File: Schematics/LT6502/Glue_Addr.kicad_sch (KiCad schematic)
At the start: 28 parts, among them IC1 ATF1508AS-7AX100, J1 Conn_02x05_Odd_Even, X1 28.322MHz

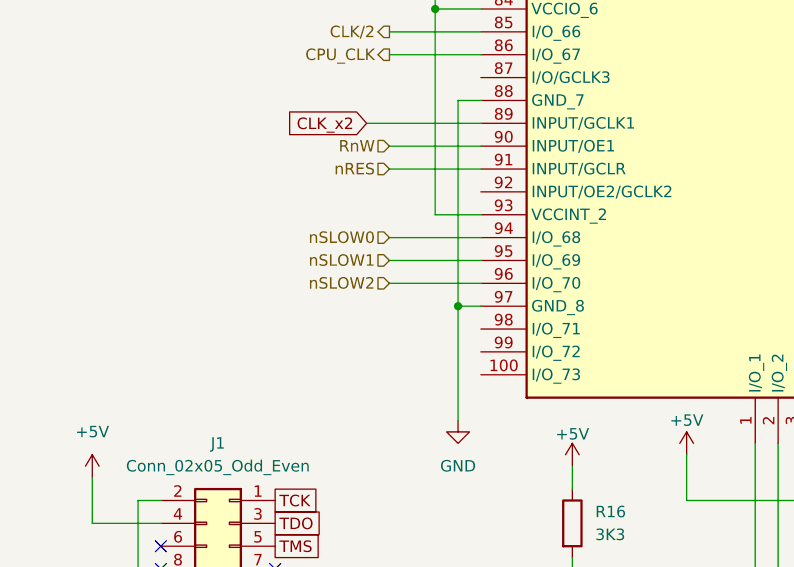
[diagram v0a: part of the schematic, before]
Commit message: Tweaks to Schematics
Shrunk main PCB
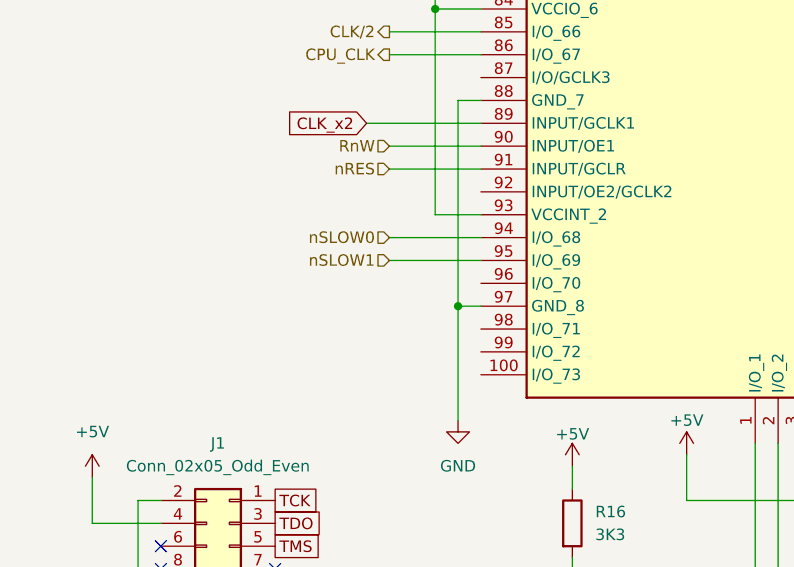
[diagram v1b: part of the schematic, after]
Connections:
- net nSLOW2: no longer names the net of IC1.96 (I/O_70)
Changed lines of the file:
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@@
-	(wire
-		(pts
-			(xy 57.15 97.79) (xy 67.31 97.79)
-		)
-		(stroke
-			(width 0)
-			(type default)
-		)
-	)
 	(wire
 		(pts
@@
 		)
 	)
-	(hierarchical_label "nSLOW2"
-		(shape input)
-		(at 57.15 97.79 180)
-		(effects
-			(font
-				(size 1.27 1.27)
-			)
-			(justify right)
-		)
-	)

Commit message: Further work on Schematics, All parts placed on PCB
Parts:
- J1: footprint Connector_PinHeader_2.54mm:PinHeader_2x05_P2.54mm_Vertical -> Connector_PinHeader_2.54mm:PinHeader_2x05_P2.54mm_Horizontal
- R14, R15, R16, R17, R18, R19, R20, R21, R22, R23, R24, R25, R26, R27, R28: footprint Resistor_SMD:R_0603_1608Metric_Pad0.98x0.95mm_HandSolder -> Resistor_SMD:R_0402_1005Metric
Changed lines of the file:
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@@
 			)
 		)
-		(property "Footprint" "Resistor_SMD:R_0603_1608Metric_Pad0.98x0.95mm_HandSolder"
+		(property "Footprint" "Resistor_SMD:R_0402_1005Metric"
 			(at 229.362 50.8 90)
 			(effects
@@
 			)
 		)
-		(property "Footprint" "Resistor_SMD:R_0603_1608Metric_Pad0.98x0.95mm_HandSolder"
+		(property "Footprint" "Resistor_SMD:R_0402_1005Metric"
 			(at 136.652 137.16 90)
 			(effects
@@
 			)
 		)
-		(property "Footprint" "Resistor_SMD:R_0603_1608Metric_Pad0.98x0.95mm_HandSolder"
+		(property "Footprint" "Resistor_SMD:R_0402_1005Metric"
 			(at 235.712 115.57 90)
 			(effects
@@
 			)
 		)
-		(property "Footprint" "Resistor_SMD:R_0603_1608Metric_Pad0.98x0.95mm_HandSolder"
+		(property "Footprint" "Resistor_SMD:R_0402_1005Metric"
 			(at 179.832 151.13 90)
 			(effects
@@
 			)
 		)
-		(property "Footprint" "Connector_PinHeader_2.54mm:PinHeader_2x05_P2.54mm_Vertical"
+		(property "Footprint" "Connector_PinHeader_2.54mm:PinHeader_2x05_P2.54mm_Horizontal"
 			(at 39.37 127 0)
 			(effects
@@
 			)
 		)
-		(property "Footprint" "Resistor_SMD:R_0603_1608Metric_Pad0.98x0.95mm_HandSolder"
+		(property "Footprint" "Resistor_SMD:R_0402_1005Metric"
 			(at 75.692 124.46 90)
 			(effects
@@
 			)
 		)
-		(property "Footprint" "Resistor_SMD:R_0603_1608Metric_Pad0.98x0.95mm_HandSolder"
+		(property "Footprint" "Resistor_SMD:R_0402_1005Metric"
 			(at 214.122 50.8 90)
 			(effects
@@
 			)
 		)
-		(property "Footprint" "Resistor_SMD:R_0603_1608Metric_Pad0.98x0.95mm_HandSolder"
+		(property "Footprint" "Resistor_SMD:R_0402_1005Metric"
 			(at 132.842 157.48 90)
 			(effects
@@
 			)
 		)
-		(property "Footprint" "Resistor_SMD:R_0603_1608Metric_Pad0.98x0.95mm_HandSolder"
+		(property "Footprint" "Resistor_SMD:R_0402_1005Metric"
 			(at 225.552 115.57 90)
 			(effects
@@
 			)
 		)
-		(property "Footprint" "Resistor_SMD:R_0603_1608Metric_Pad0.98x0.95mm_HandSolder"
+		(property "Footprint" "Resistor_SMD:R_0402_1005Metric"
 			(at 50.038 43.18 90)
 			(effects
@@
 			)
 		)
-		(property "Footprint" "Resistor_SMD:R_0603_1608Metric_Pad0.98x0.95mm_HandSolder"
+		(property "Footprint" "Resistor_SMD:R_0402_1005Metric"
 			(at 203.962 50.8 90)
 			(effects
@@
 			)
 		)
-		(property "Footprint" "Resistor_SMD:R_0603_1608Metric_Pad0.98x0.95mm_HandSolder"
+		(property "Footprint" "Resistor_SMD:R_0402_1005Metric"
 			(at 215.392 115.57 90)
 			(effects
@@
 			)
 		)
-		(property "Footprint" "Resistor_SMD:R_0603_1608Metric_Pad0.98x0.95mm_HandSolder"
+		(property "Footprint" "Resistor_SMD:R_0402_1005Metric"
 			(at 24.638 165.1 90)
 			(effects
@@
 			)
 		)
-		(property "Footprint" "Resistor_SMD:R_0603_1608Metric_Pad0.98x0.95mm_HandSolder"
+		(property "Footprint" "Resistor_SMD:R_0402_1005Metric"
 			(at 167.132 151.13 90)
 			(effects
@@
 			)
 		)
-		(property "Footprint" "Resistor_SMD:R_0603_1608Metric_Pad0.98x0.95mm_HandSolder"
+		(property "Footprint" "Resistor_SMD:R_0402_1005Metric"
 			(at 243.332 50.8 90)
 			(effects
@@
 			)
 		)
-		(property "Footprint" "Resistor_SMD:R_0603_1608Metric_Pad0.98x0.95mm_HandSolder"
+		(property "Footprint" "Resistor_SMD:R_0402_1005Metric"
 			(at 253.492 50.8 90)
 			(effects

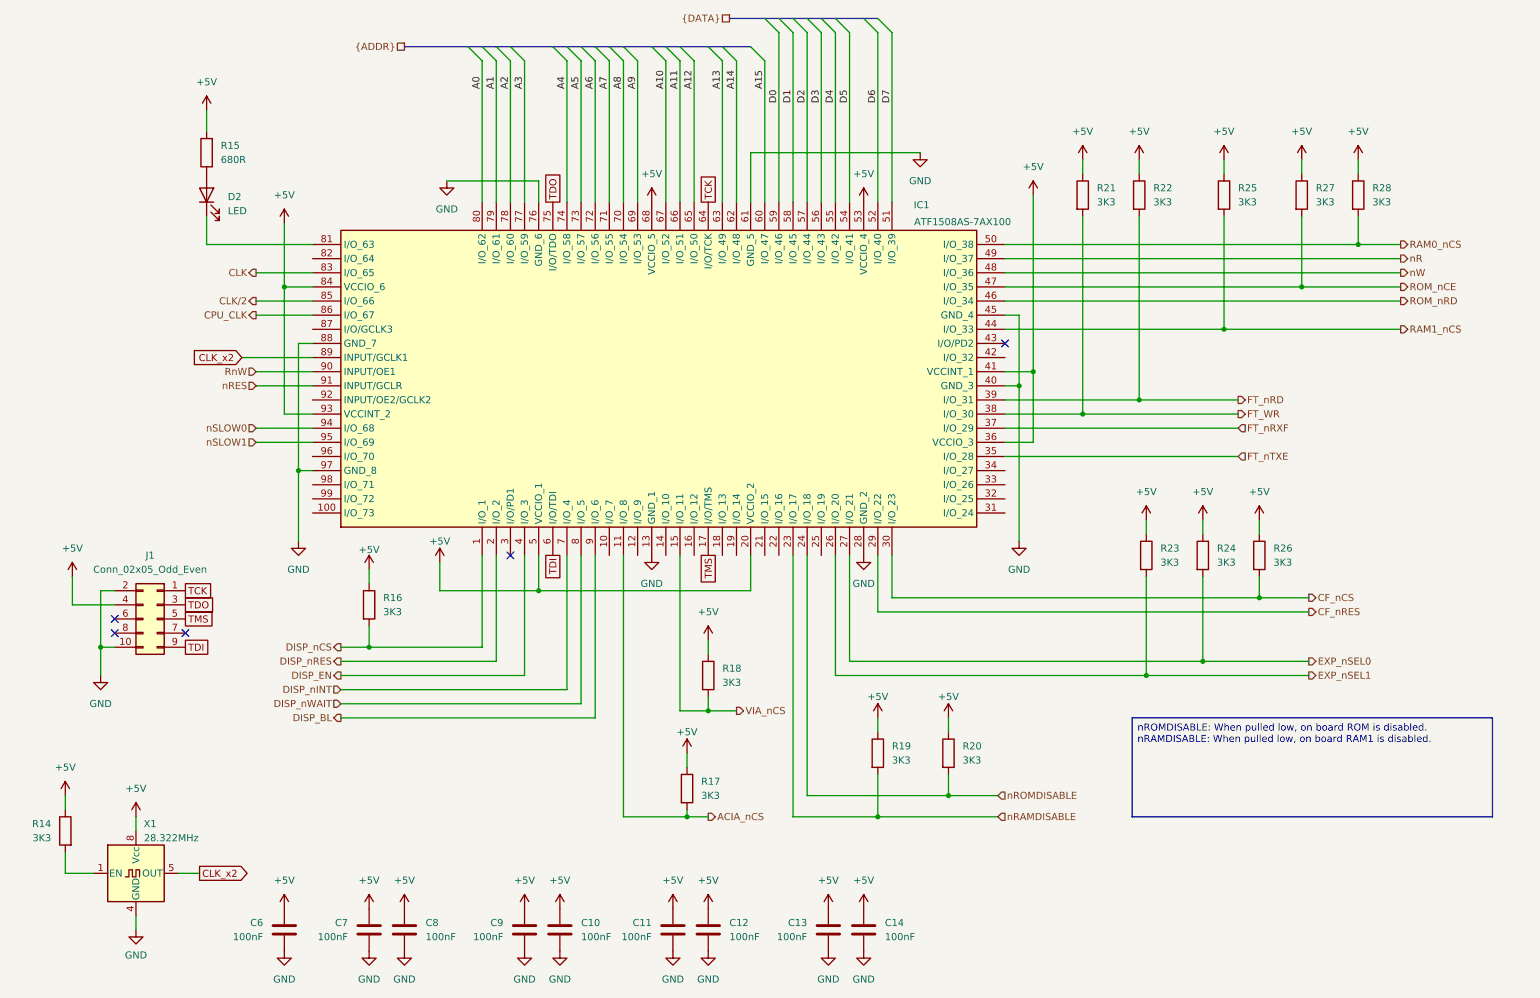
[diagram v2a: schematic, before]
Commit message: Updated main board and started keybed
main board a bit wider due to keybed width
created keybed, begun routing
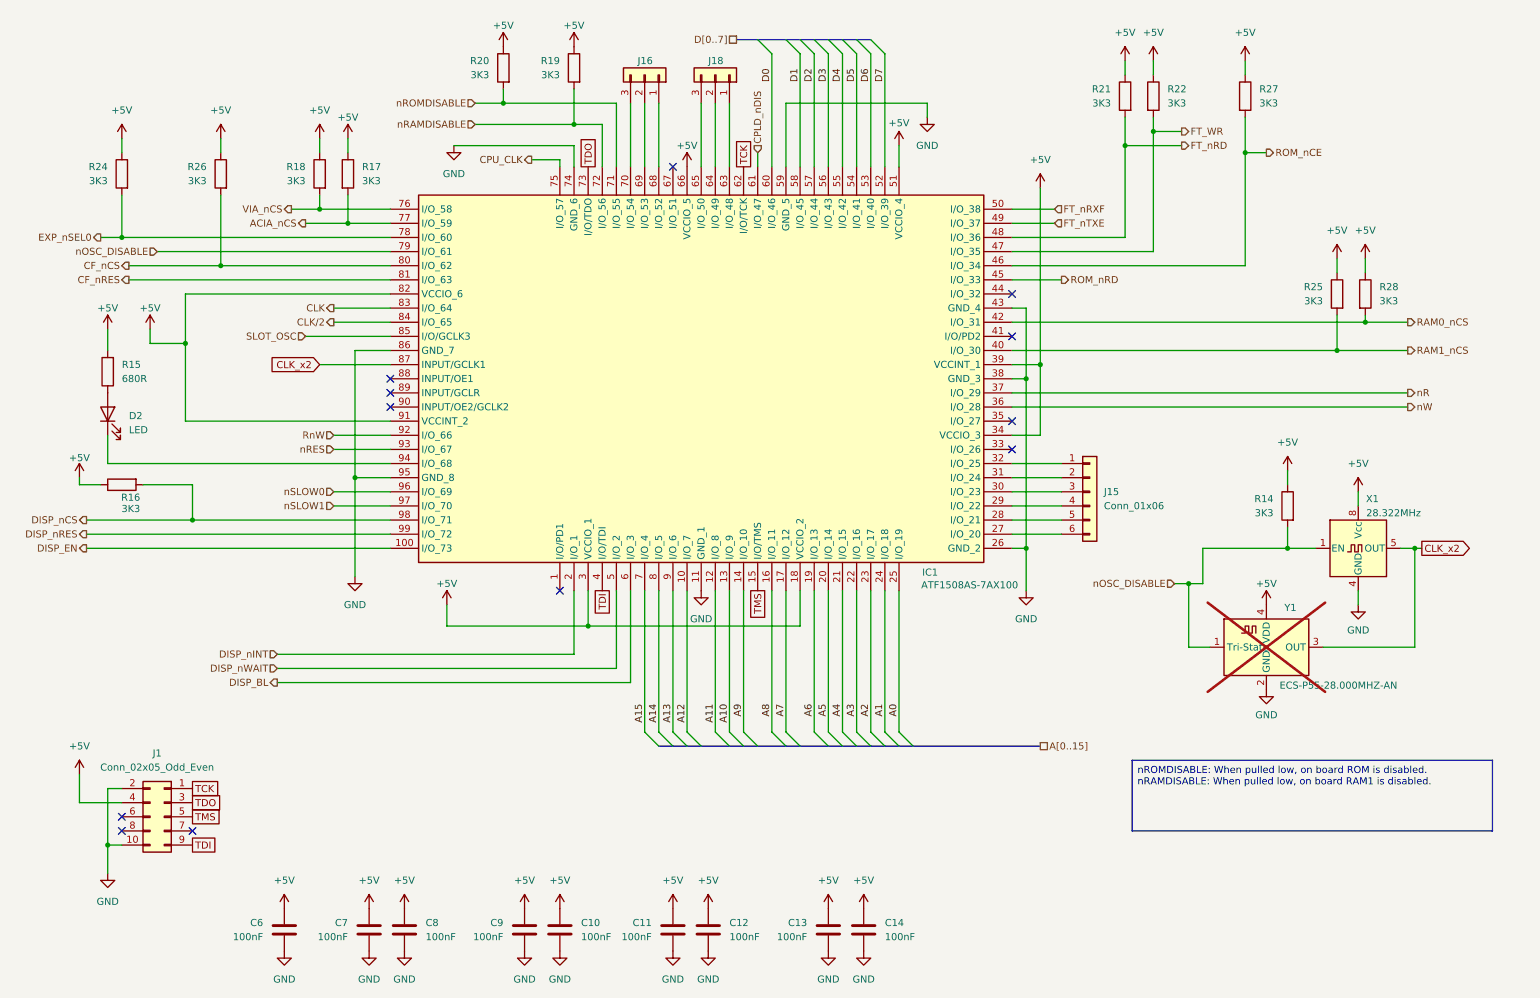
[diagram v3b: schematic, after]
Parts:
- removed IC1: ATF1508AS-7AX100, ATF1508AS-10QU100:QFP65P1720X2320X340-100N, symbol ATF1508AS-10QU100:ATF1508AS-10QU100
- removed R23: 3K3, Resistor_SMD:R_0402_1005Metric, symbol Device:R
- added IC1: ATF1508AS-7AX100, ATF1508ASL-nnAU100:QFP50P1600X1600X120-100N, symbol ATF1508ASL-25AU100:ATF1508ASL-25AU100
- added J15: Conn_01x06, Connector_PinHeader_1.00mm:PinHeader_1x06_P1.00mm_Vertical_SMD_Pin1Left, symbol Connector_Generic:Conn_01x06
- added J16, J18: Conn_01x03, Connector_PinHeader_1.00mm:PinHeader_1x03_P1.00mm_Vertical_SMD_Pin1Left, symbol Connector_Generic:Conn_01x03
- added Y1: ECS-P55-28.000MHZ-AN, Oscillator:Oscillator_SMD_EuroQuartz_XO53-4Pin_5.0x3.2mm, symbol Oscillator:ECS-2520MV-xxx-xx
- C10: footprint Capacitor_SMD:C_0603_1608Metric -> Capacitor_SMD:C_0402_1005Metric
- X1: Mouser Part Number (none) -> 520-2100AX-283.2
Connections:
- net +5V: now also IC1.18 (VCCIO_2), IC1.3 (VCCIO_1), IC1.34 (VCCIO_3), IC1.39 (VCCINT_1), IC1.51 (VCCIO_4), IC1.66 (VCCIO_5), IC1.82 (VCCIO_6), IC1.91 (VCCINT_2), Y1.4 (VDD)
- net A0: now also IC1.25 (I/O_19)
- net A1: now also IC1.24 (I/O_18)
- net A10: now also IC1.13 (I/O_9)
- net A11: now also IC1.12 (I/O_8)
- net A12: now also IC1.10 (I/O_7)
- net A13: now also IC1.9 (I/O_6)
- net A14: now also IC1.8 (I/O_5)
- net A15: now also IC1.7 (I/O_4)
- net A2: now also IC1.23 (I/O_17)
- net A3: now also IC1.22 (I/O_16)
- net A4: now also IC1.21 (I/O_15)
- net A5: now also IC1.20 (I/O_14)
- net A6: now also IC1.19 (I/O_13)
- net A7: now also IC1.17 (I/O_12)
- net A8: now also IC1.16 (I/O_11)
- net A9: now also IC1.14 (I/O_10)
- net ACIA_nCS: now also IC1.77 (I/O_59)
- net CF_nCS: now also IC1.80 (I/O_62)
- net CF_nRES: now also IC1.81 (I/O_63)
- net CLK: now also IC1.83 (I/O_64)
- net CLK_x2: now also IC1.87 (INPUT/GCLK1), Y1.3 (OUT)
- net CLK/2: now also IC1.84 (I/O_65)
- net CPU_CLK: now also IC1.75 (I/O_57)
- net D0: now also IC1.60 (I/O_46)
- net D1: now also IC1.58 (I/O_45)
- net D2: now also IC1.57 (I/O_44)
- net D3: now also IC1.56 (I/O_43)
- net D4: now also IC1.55 (I/O_42)
- net D5: now also IC1.54 (I/O_41)
- net D6: now also IC1.53 (I/O_40)
- net D7: now also IC1.52 (I/O_39)
- net DISP_BL: now also IC1.6 (I/O_3)
- net DISP_EN: now also IC1.100 (I/O_73)
- net DISP_nCS: now also IC1.98 (I/O_71)
- net DISP_nINT: now also IC1.2 (I/O_1)
- net DISP_nRES: now also IC1.99 (I/O_72)
- net DISP_nWAIT: now also IC1.5 (I/O_2)
- net EXP_nSEL0: now also IC1.78 (I/O_60)
- net FT_WR: now also R22.2, IC1.47 (I/O_35); no longer R21.2
- net FT_nRD: now also R21.2, IC1.48 (I/O_36); no longer R22.2
- net FT_nRXF: now also IC1.50 (I/O_38)
- net FT_nTXE: now also IC1.49 (I/O_37)
- net GND: now also IC1.11 (GND_1), IC1.26 (GND_2), IC1.38 (GND_3), IC1.43 (GND_4), IC1.59 (GND_5), IC1.74 (GND_6), IC1.86 (GND_7), IC1.95 (GND_8), Y1.2 (GND)
- net RAM0_nCS: now also IC1.42 (I/O_31)
- net RAM1_nCS: now also IC1.40 (I/O_30)
- net ROM_nCE: now also IC1.46 (I/O_34)
- net ROM_nRD: now also IC1.45 (I/O_33)
- net RnW: now also IC1.92 (I/O_66)
- net TCK: now also IC1.62 (I/O/TCK)
- net TDI: now also IC1.4 (I/O/TDI)
- net TDO: now also IC1.73 (I/O/TDO)
- net TMS: now also IC1.15 (I/O/TMS)
- net VIA_nCS: now also IC1.76 (I/O_58)
- net nR: now also IC1.37 (I/O_29)
- net nRAMDISABLE: now also IC1.72 (I/O_56)
- net nRES: now also IC1.93 (I/O_67)
- net nROMDISABLE: now also IC1.71 (I/O_55)
- net nSLOW0: now also IC1.96 (I/O_69)
- net nSLOW1: now also IC1.97 (I/O_70)
- net nW: now also IC1.36 (I/O_28)
- net at D2.1 (K): now also IC1.94 (I/O_68)
- net nOSC_DISABLE: now reaches R14.2, X1.1 (EN)
- net nOSC_DISABLE: now also IC1.79 (I/O_61), Y1.1 (Tri-State)
- new net: IC1.68 (I/O_52), J16.1 (Pin_1)
- new net: IC1.69 (I/O_53), J16.2 (Pin_2)
- new net: IC1.70 (I/O_54), J16.3 (Pin_3)
- new net: IC1.27 (I/O_20), J15.6 (Pin_6)
- new net: IC1.28 (I/O_21), J15.5 (Pin_5)
- new net: IC1.29 (I/O_22), J15.4 (Pin_4)
- new net: IC1.30 (I/O_23), J15.3 (Pin_3)
- new net: IC1.31 (I/O_24), J15.2 (Pin_2)
- new net: IC1.32 (I/O_25), J15.1 (Pin_1)
- new net: IC1.63 (I/O_48), J18.1 (Pin_1)
- new net: IC1.64 (I/O_49), J18.2 (Pin_2)
- new net: IC1.65 (I/O_50), J18.3 (Pin_3)
- new net CPLD_nDIS: IC1.61 (I/O_47)
- new net SLOT_OSC: IC1.85 (I/O/GCLK3)
- no-connect marks 5 -> 12
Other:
- moved on the sheet: D2, J1, R14, R15, R16, R17, R18, R19, R20, R21, R22, R24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

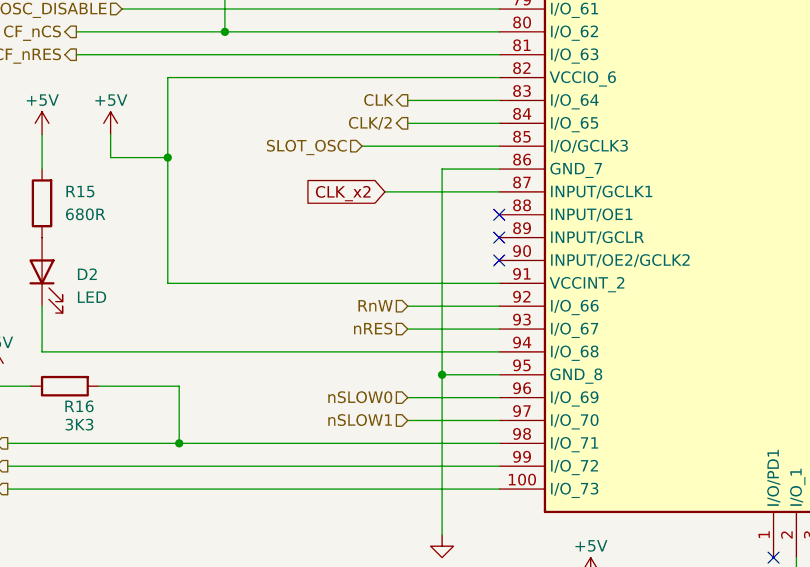
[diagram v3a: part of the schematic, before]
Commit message: Added speaker
Added a simple LM386/speaker and link to CPLD for simple audio.
Updated step files
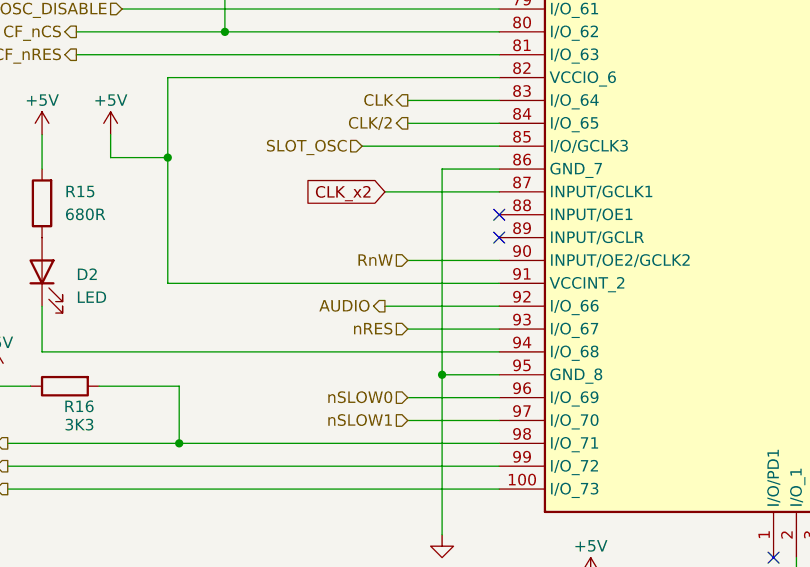
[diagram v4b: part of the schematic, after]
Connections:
- net RnW: now also IC1.90 (INPUT/OE2/GCLK2); no longer IC1.92 (I/O_66)
- new net AUDIO: IC1.92 (I/O_66)
- no-connect marks 12 -> 11
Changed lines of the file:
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@@
+	)
+	(no_connect
+		(at 132.08 45.72)
 	)
 	(no_connect
@@
 	)
 	(no_connect
-		(at 81.28 88.9)
-	)
-	(no_connect
 		(at 193.04 68.58)
-	)
-	(no_connect
-		(at 132.08 45.72)
 	)
 	(no_connect
@@
 	(wire
 		(pts
+			(xy 68.58 93.98) (xy 81.28 93.98)
+		)
+		(stroke
+			(width 0)
+			(type default)
+		)
+	)
+	(wire
+		(pts
 			(xy 193.04 53.34) (xy 200.66 53.34)
 		)
@@
 	(wire
 		(pts
-			(xy 71.12 93.98) (xy 81.28 93.98)
+			(xy 71.12 88.9) (xy 81.28 88.9)
 		)
 		(stroke
@@
 		)
 	)
+	(hierarchical_label "AUDIO"
+		(shape output)
+		(at 68.58 93.98 180)
+		(effects
+			(font
+				(size 1.27 1.27)
+			)
+			(justify right)
+		)
+	)
 	(hierarchical_label "RnW"
 		(shape input)
-		(at 71.12 93.98 180)
-		(effects
-			(font
+		(at 71.12 88.9 180)
+		(effects
+			(font
